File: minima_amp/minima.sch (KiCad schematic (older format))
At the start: 40 parts, among them J1 input, J2 output, J3 powersupply, U1 LM1875

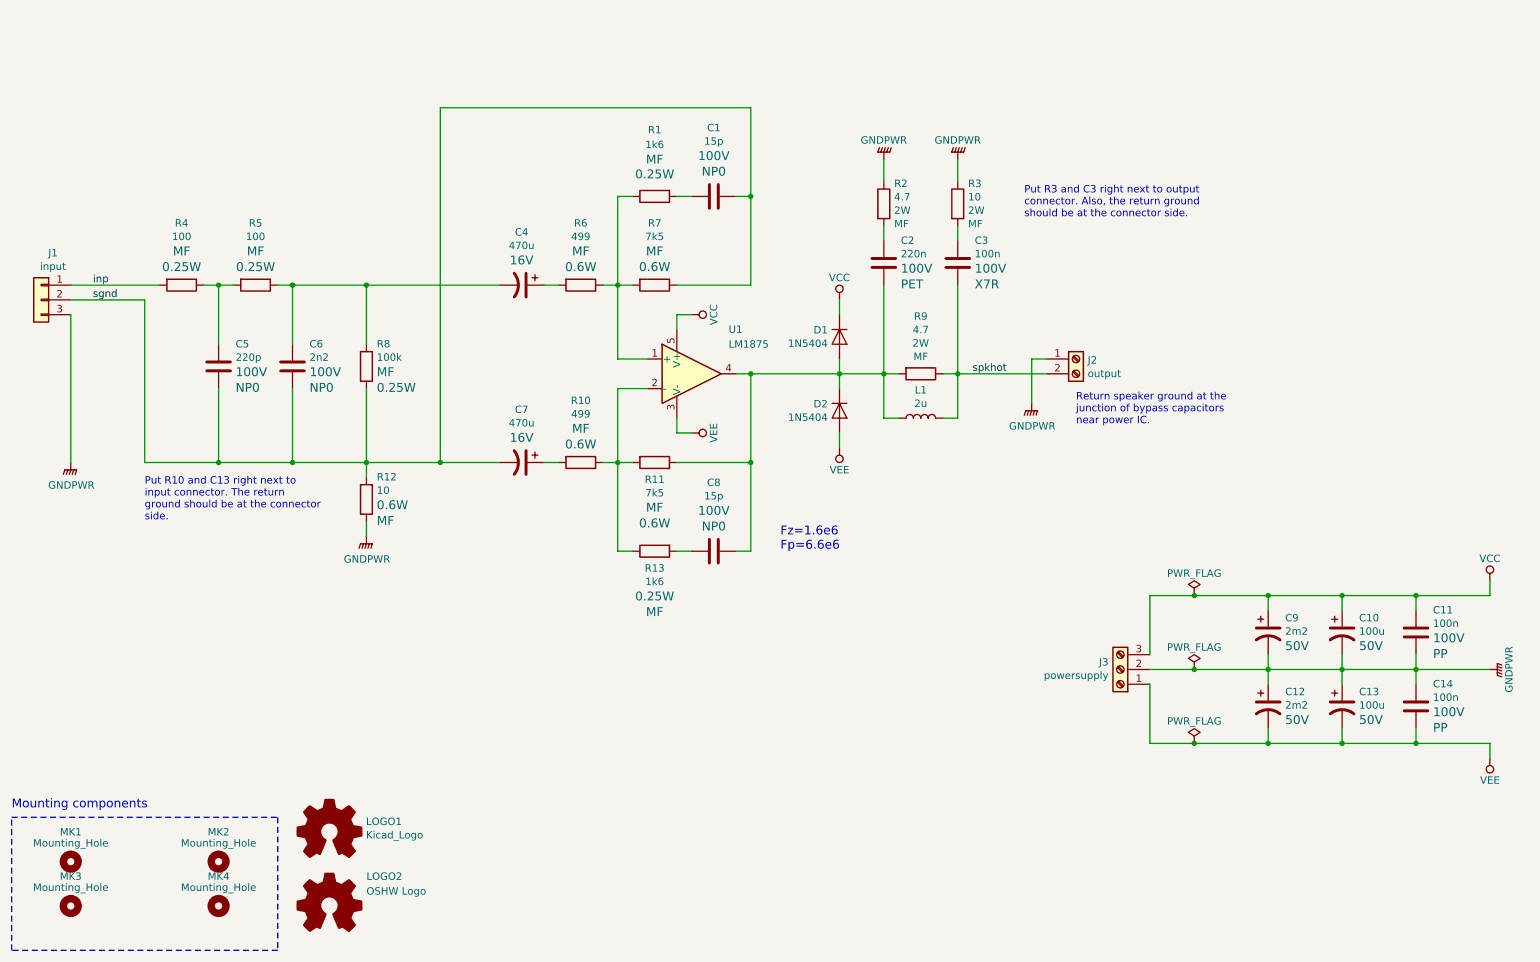
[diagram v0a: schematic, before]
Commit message: Using designators as specified in README.rst
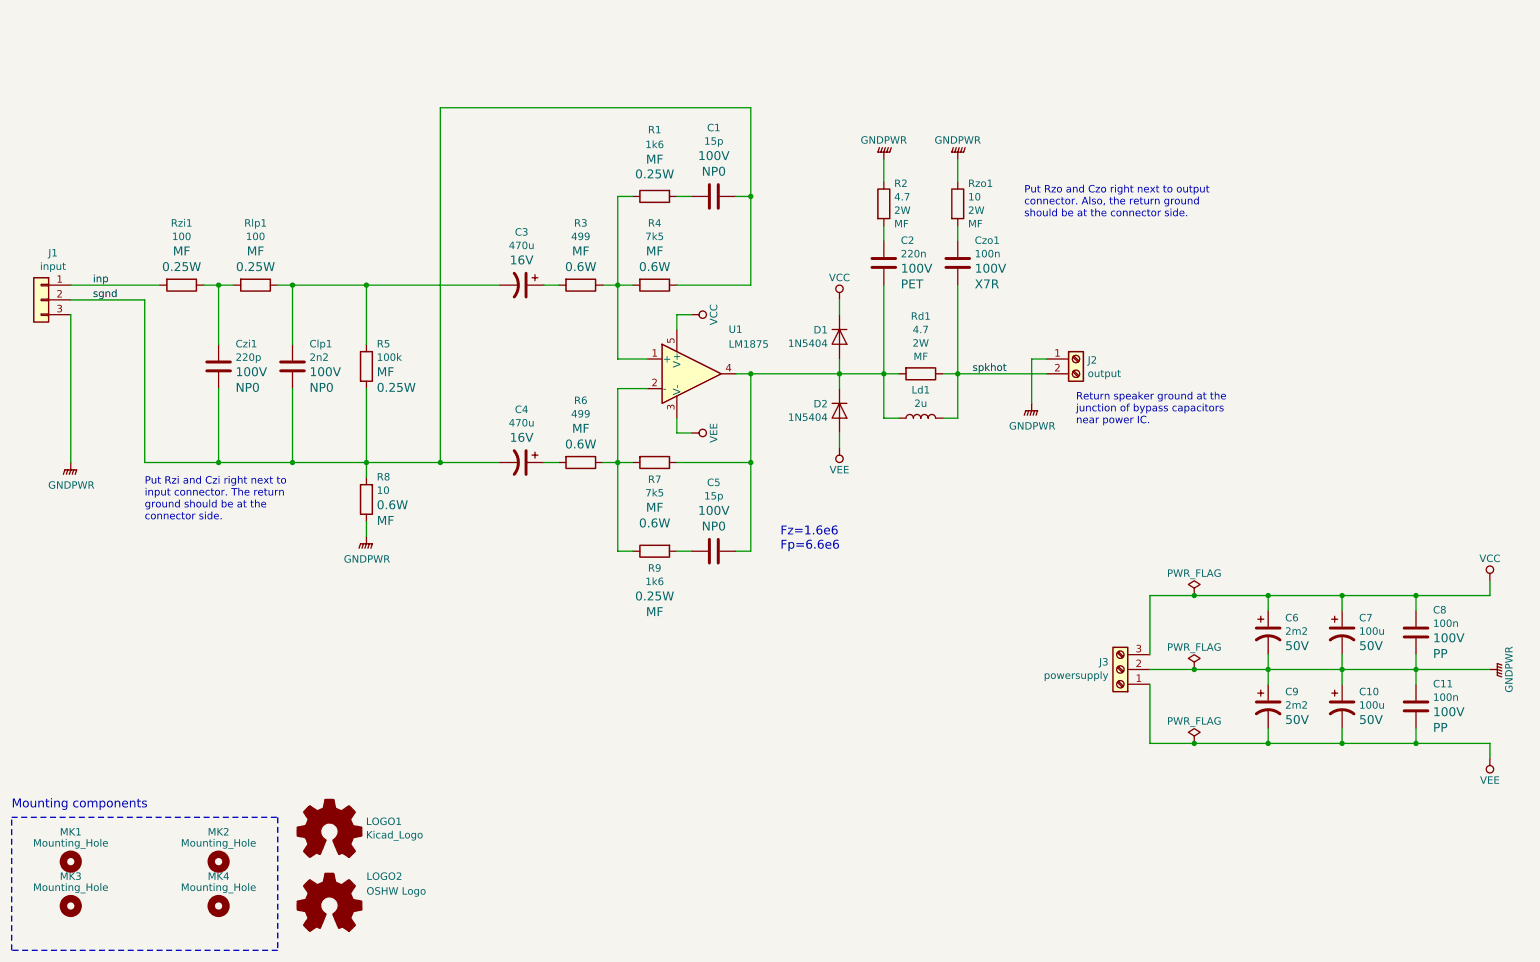
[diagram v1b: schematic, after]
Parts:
- renumbered C13 to C10, C14 to C11, C4 to C3, C7 to C4, C8 to C5, C9 to C6, C10 to C7, C11 to C8, C12 to C9, C6 to Clp1, C5 to Czi1, C3 to Czo1, L1 to Ld1, R6 to R3, R7 to R4, R8 to R5, R10 to R6, R11 to R7, R12 to R8, R13 to R9, R9 to Rd1, R5 to Rlp1, R4 to Rzi1, R3 to Rzo1
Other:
- note added: "Put Rzi and Czi right next to\ninput connector. The return\nground should be at the\nconnector side."
- note added: "Put Rzo and Czo right next to output \nconnector. Also, the return ground \nshould be at the connector side."
- note removed: "Put R10 and C13 right next to\ninput connector. The return\nground should be at the connector\nside."
- note removed: "Put R3 and C3 right next to output \nconnector. Also, the return ground \nshould be at the connector side."
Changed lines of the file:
@@
 Return speaker ground at the\njunction of bypass capacitors \nnear power IC.
 $Comp
-L Device:C C?
+L Device:C Clp?
 U 1 1 5B6E6214
 P 2700 3550
-AR Path="/5B57B0FA/5B6E6214" Ref="C?"  Part="1"
-AR Path="/5B6E6214" Ref="C6"  Part="1"
-F 0 "C6" H 2815 3702 50  0000 L CNN
+AR Path="/5B57B0FA/5B6E6214" Ref="Clp?"  Part="1"
+AR Path="/5B6E6214" Ref="Clp1"  Part="1"
+F 0 "Clp1" H 2815 3702 50  0000 L CNN
 F 1 "2n2" H 2815 3611 50  0000 L CNN
 F 2 "Capacitor_THT:C_Disc_D4.3mm_W1.9mm_P5.00mm" H 2738 3400 50  0001 C CNN
@@
 $EndComp
 $Comp
-L Device:C C?
+L Device:C Czi?
 U 1 1 5B6E621F
 P 2200 3550
-AR Path="/5B57B0FA/5B6E621F" Ref="C?"  Part="1"
-AR Path="/5B6E621F" Ref="C5"  Part="1"
-F 0 "C5" H 2315 3702 50  0000 L CNN
+AR Path="/5B57B0FA/5B6E621F" Ref="Czi?"  Part="1"
+AR Path="/5B6E621F" Ref="Czi1"  Part="1"
+F 0 "Czi1" H 2315 3702 50  0000 L CNN
 F 1 "220p" H 2315 3611 50  0000 L CNN
 F 2 "Capacitor_THT:C_Disc_D4.3mm_W1.9mm_P5.00mm" H 2238 3400 50  0001 C CNN
@@
 $EndComp
 $Comp
-L Device:R R?
+L Device:R Rzi?
 U 1 1 5B6E622C
 P 1950 3000
-AR Path="/5B57B0FA/5B6E622C" Ref="R?"  Part="1"
-AR Path="/5B6E622C" Ref="R4"  Part="1"
-F 0 "R4" V 1531 3000 50  0000 C CNN
+AR Path="/5B57B0FA/5B6E622C" Ref="Rzi?"  Part="1"
+AR Path="/5B6E622C" Ref="Rzi1"  Part="1"
+F 0 "Rzi1" V 1531 3000 50  0000 C CNN
 F 1 "100" V 1622 3000 50  0000 C CNN
 F 2 "Resistor_THT:R_Axial_DIN0207_L6.3mm_D2.5mm_P10.16mm_Horizontal" V 1880 3000 50  0001 C CNN
@@
 $EndComp
 $Comp
-L Device:R R?
+L Device:R Rlp?
 U 1 1 5B6E6237
 P 2450 3000
-AR Path="/5B57B0FA/5B6E6237" Ref="R?"  Part="1"
-AR Path="/5B6E6237" Ref="R5"  Part="1"
-F 0 "R5" V 2031 3000 50  0000 C CNN
+AR Path="/5B57B0FA/5B6E6237" Ref="Rlp?"  Part="1"
+AR Path="/5B6E6237" Ref="Rlp1"  Part="1"
+F 0 "Rlp1" V 2031 3000 50  0000 C CNN
 F 1 "100" V 2122 3000 50  0000 C CNN
 F 2 "Resistor_THT:R_Axial_DIN0207_L6.3mm_D2.5mm_P10.16mm_Horizontal" V 2380 3000 50  0001 C CNN
@@
 P 3200 4450
 AR Path="/5B57B0FA/5B6E6242" Ref="R?"  Part="1"
-AR Path="/5B6E6242" Ref="R12"  Part="1"
-F 0 "R12" H 3130 4298 50  0000 R CNN
+AR Path="/5B6E6242" Ref="R8"  Part="1"
+F 0 "R8" H 3130 4298 50  0000 R CNN
 F 1 "10" H 3130 4389 50  0000 R CNN
 F 2 "Resistor_THT:R_Axial_DIN0207_L6.3mm_D2.5mm_P10.16mm_Horizontal" V 3130 4450 50  0001 C CNN
@@
 P 3200 3550
 AR Path="/5B57B0FA/5B6E625B" Ref="R?"  Part="1"
-AR Path="/5B6E625B" Ref="R8"  Part="1"
-F 0 "R8" H 3270 3702 50  0000 L CNN
+AR Path="/5B6E625B" Ref="R5"  Part="1"
+F 0 "R5" H 3270 3702 50  0000 L CNN
 F 1 "100k" H 3270 3611 50  0000 L CNN
 F 2 "Resistor_THT:R_Axial_DIN0207_L6.3mm_D2.5mm_P10.16mm_Horizontal" V 3130 3550 50  0001 C CNN
@@
 $EndComp
 Text Notes 1700 4600 0    50   ~ 0
-Put R10 and C13 right next to\ninput connector. The return\nground should be at the connector\nside.
+Put Rzi and Czi right next to\ninput connector. The return\nground should be at the\nconnector side.
 Text Label 1350 3100 0    50   ~ 0
 sgnd
@@
 P 10300 5350
 AR Path="/5ABAAF3C/5B6EB783" Ref="C?"  Part="1"
-AR Path="/5B6EB783" Ref="C11"  Part="1"
-F 0 "C11" H 10415 5502 50  0000 L CNN
+AR Path="/5B6EB783" Ref="C8"  Part="1"
+F 0 "C8" H 10415 5502 50  0000 L CNN
 F 1 "100n" H 10415 5411 50  0000 L CNN
 F 2 "Capacitor_THT:C_Rect_L7.0mm_W3.5mm_P5.00mm" H 10338 5200 50  0001 C CNN
@@
 P 9800 5350
 AR Path="/5ABAAF3C/5B6EB78D" Ref="C?"  Part="1"
-AR Path="/5B6EB78D" Ref="C10"  Part="1"
-F 0 "C10" H 9915 5449 50  0000 L CNN
+AR Path="/5B6EB78D" Ref="C7"  Part="1"
+F 0 "C7" H 9915 5449 50  0000 L CNN
 F 1 "100u" H 9915 5358 50  0000 L CNN
 F 2 "Capacitor_THT:CP_Radial_D8.0mm_P3.50mm" H 9800 5350 50  0001 C CNN
@@
 P 10300 5850
 AR Path="/5ABAAF3C/5B6EB7B5" Ref="C?"  Part="1"
-AR Path="/5B6EB7B5" Ref="C14"  Part="1"
-F 0 "C14" H 10415 6002 50  0000 L CNN
+AR Path="/5B6EB7B5" Ref="C11"  Part="1"
+F 0 "C11" H 10415 6002 50  0000 L CNN
 F 1 "100n" H 10415 5911 50  0000 L CNN
 F 2 "Capacitor_THT:C_Rect_L7.0mm_W3.5mm_P5.00mm" H 10338 5700 50  0001 C CNN
@@
 P 9800 5850
 AR Path="/5ABAAF3C/5B6EB7BF" Ref="C?"  Part="1"
-AR Path="/5B6EB7BF" Ref="C13"  Part="1"
-F 0 "C13" H 9915 5949 50  0000 L CNN
+AR Path="/5B6EB7BF" Ref="C10"  Part="1"
+F 0 "C10" H 9915 5949 50  0000 L CNN
 F 1 "100u" H 9915 5858 50  0000 L CNN
 F 2 "Capacitor_THT:CP_Radial_D8.0mm_P3.50mm" H 9800 5850 50  0001 C CNN
@@
 P 9300 5350
 AR Path="/5ABAAF67/5B6EC2C2" Ref="C?"  Part="1"
-AR Path="/5B6EC2C2" Ref="C9"  Part="1"
-F 0 "C9" H 9415 5449 50  0000 L CNN
+AR Path="/5B6EC2C2" Ref="C6"  Part="1"
+F 0 "C6" H 9415 5449 50  0000 L CNN
 F 1 "2m2" H 9415 5358 50  0000 L CNN
 F 2 "Capacitor_THT:CP_Radial_D16.0mm_P7.50mm" H 9300 5350 50  0001 C CNN
@@
 P 9300 5850
 AR Path="/5ABAAF67/5B6EC310" Ref="C?"  Part="1"
-AR Path="/5B6EC310" Ref="C12"  Part="1"
-F 0 "C12" H 9415 5949 50  0000 L CNN
+AR Path="/5B6EC310" Ref="C9"  Part="1"
+F 0 "C9" H 9415 5949 50  0000 L CNN
 F 1 "2m2" H 9415 5858 50  0000 L CNN
 F 2 "Capacitor_THT:CP_Radial_D16.0mm_P7.50mm" H 9300 5850 50  0001 C CNN
@@
 $EndComp
 $Comp
-L Device:R R?
+L Device:R Rd?
 U 1 1 5B6FAE68
 P 6950 3600
-AR Path="/5ABAAF3C/5B6FAE68" Ref="R?"  Part="1"
-AR Path="/5B6FAE68" Ref="R9"  Part="1"
-F 0 "R9" V 6561 3600 50  0000 C CNN
+AR Path="/5ABAAF3C/5B6FAE68" Ref="Rd?"  Part="1"
+AR Path="/5B6FAE68" Ref="Rd1"  Part="1"
+F 0 "Rd1" V 6561 3600 50  0000 C CNN
 F 1 "4.7" V 6652 3600 50  0000 C CNN
 F 2 "Resistor_THT:R_Axial_DIN0411_L9.9mm_D3.6mm_P15.24mm_Horizontal" V 6880 3600 50  0001 C CNN
@@
 $EndComp
 $Comp
-L Device:L L?
+L Device:L Ld?
 U 1 1 5B6FAE6F
 P 6950 3900
-AR Path="/5ABAAF3C/5B6FAE6F" Ref="L?"  Part="1"
-AR Path="/5B6FAE6F" Ref="L1"  Part="1"
-F 0 "L1" V 7140 3900 50  0000 C CNN
+AR Path="/5ABAAF3C/5B6FAE6F" Ref="Ld?"  Part="1"
+AR Path="/5B6FAE6F" Ref="Ld1"  Part="1"
+F 0 "Ld1" V 7140 3900 50  0000 C CNN
 F 1 "2u" V 7049 3900 50  0000 C CNN
 F 2 "Inductor_THT:L_Axial_L12.0mm_D5.0mm_P15.24mm_Horizontal_Fastron_MISC" H 6950 3900 50  0001 C CNN
@@
 	6700 3900 6800 3900
 $Comp
-L Device:R R?
+L Device:R Rzo?
 U 1 1 5B6FAE7C
 P 7200 2450
-AR Path="/5ABAAF3C/5B6FAE7C" Ref="R?"  Part="1"
-AR Path="/5B6FAE7C" Ref="R3"  Part="1"
-F 0 "R3" H 7270 2587 50  0000 L CNN
+AR Path="/5ABAAF3C/5B6FAE7C" Ref="Rzo?"  Part="1"
+AR Path="/5B6FAE7C" Ref="Rzo1"  Part="1"
+F 0 "Rzo1" H 7270 2587 50  0000 L CNN
 F 1 "10" H 7270 2496 50  0000 L CNN
 F 2 "Resistor_THT:R_Axial_DIN0411_L9.9mm_D3.6mm_P15.24mm_Horizontal" V 7130 2450 50  0001 C CNN
@@
 P 4250 3000
 AR Path="/5ABAAF3C/5B6FAE98" Ref="C?"  Part="1"
-AR Path="/5B6FAE98" Ref="C4"  Part="1"
-F 0 "C4" V 3892 3000 50  0000 C CNN
+AR Path="/5B6FAE98" Ref="C3"  Part="1"
+F 0 "C3" V 3892 3000 50  0000 C CNN
 F 1 "470u" V 3983 3000 50  0000 C CNN
 F 2 "Capacitor_THT:CP_Radial_D8.0mm_P3.50mm" H 4250 3000 50  0001 C CNN
@@
 P 5150 4800
 AR Path="/5ABAAF3C/5B6FAEAE" Ref="R?"  Part="1"
-AR Path="/5B6FAEAE" Ref="R13"  Part="1"
-F 0 "R13" V 5265 4800 50  0000 C CNN
+AR Path="/5B6FAEAE" Ref="R9"  Part="1"
+F 0 "R9" V 5265 4800 50  0000 C CNN
 F 1 "1k6" V 5356 4800 50  0000 C CNN
 F 2 "Resistor_THT:R_Axial_DIN0207_L6.3mm_D2.5mm_P10.16mm_Horizontal" V 5080 4800 50  0001 C CNN
@@
 P 5550 4800
 AR Path="/5ABAAF3C/5B6FAEC1" Ref="C?"  Part="1"
-AR Path="/5B6FAEC1" Ref="C8"  Part="1"
-F 0 "C8" V 5086 4800 50  0000 C CNN
+AR Path="/5B6FAEC1" Ref="C5"  Part="1"
+F 0 "C5" V 5086 4800 50  0000 C CNN
 F 1 "15p" V 5177 4800 50  0000 C CNN
 F 2 "Capacitor_THT:C_Disc_D3.4mm_W2.1mm_P2.50mm" H 5588 4650 50  0001 C CNN
@@
 P 4250 4200
 AR Path="/5ABAAF3C/5B6FAED8" Ref="C?"  Part="1"
-AR Path="/5B6FAED8" Ref="C7"  Part="1"
-F 0 "C7" V 3892 4200 50  0000 C CNN
+AR Path="/5B6FAED8" Ref="C4"  Part="1"
+F 0 "C4" V 3892 4200 50  0000 C CNN
 F 1 "470u" V 3983 4200 50  0000 C CNN
 F 2 "Capacitor_THT:CP_Radial_D8.0mm_P3.50mm" H 4250 4200 50  0001 C CNN
@@
 P 4650 4200
 AR Path="/5ABAAF3C/5B6FAEE5" Ref="R?"  Part="1"
-AR Path="/5B6FAEE5" Ref="R10"  Part="1"
-F 0 "R10" V 4231 4200 50  0000 C CNN
+AR Path="/5B6FAEE5" Ref="R6"  Part="1"
+F 0 "R6" V 4231 4200 50  0000 C CNN
 F 1 "499" V 4322 4200 50  0000 C CNN
 F 2 "Resistor_THT:R_Axial_DIN0207_L6.3mm_D2.5mm_P10.16mm_Horizontal" V 4580 4200 50  0001 C CNN
@@
 P 5150 3000
 AR Path="/5ABAAF3C/5B6FAEF0" Ref="R?"  Part="1"
-AR Path="/5B6FAEF0" Ref="R7"  Part="1"
-F 0 "R7" V 4731 3000 50  0000 C CNN
+AR Path="/5B6FAEF0" Ref="R4"  Part="1"
+F 0 "R4" V 4731 3000 50  0000 C CNN
 F 1 "7k5" V 4822 3000 50  0000 C CNN
 F 2 "Resistor_THT:R_Axial_DIN0207_L6.3mm_D2.5mm_P10.16mm_Horizontal" V 5080 3000 50  0001 C CNN
@@
 P 5150 4200
 AR Path="/5ABAAF3C/5B6FAEFB" Ref="R?"  Part="1"
-AR Path="/5B6FAEFB" Ref="R11"  Part="1"
-F 0 "R11" V 5265 4200 50  0000 C CNN
+AR Path="/5B6FAEFB" Ref="R7"  Part="1"
+F 0 "R7" V 5265 4200 50  0000 C CNN
 F 1 "7k5" V 5356 4200 50  0000 C CNN
 F 2 "Resistor_THT:R_Axial_DIN0207_L6.3mm_D2.5mm_P10.16mm_Horizontal" V 5080 4200 50  0001 C CNN
@@
 P 4650 3000
 AR Path="/5ABAAF3C/5B6FAF30" Ref="R?"  Part="1"
-AR Path="/5B6FAF30" Ref="R6"  Part="1"
-F 0 "R6" V 4231 3000 50  0000 C CNN
+AR Path="/5B6FAF30" Ref="R3"  Part="1"
+F 0 "R3" V 4231 3000 50  0000 C CNN
 F 1 "499" V 4322 3000 50  0000 C CNN
 F 2 "Resistor_THT:R_Axial_DIN0207_L6.3mm_D2.5mm_P10.16mm_Horizontal" V 4580 3000 50  0001 C CNN
@@
 	7200 2300 7200 2150
 $Comp
-L Device:C C?
+L Device:C Czo?
 U 1 1 5B6FAF6B
 P 7200 2850
-AR Path="/5ABAAF3C/5B6FAF6B" Ref="C?"  Part="1"
-AR Path="/5B6FAF6B" Ref="C3"  Part="1"
-F 0 "C3" H 7315 3002 50  0000 L CNN
+AR Path="/5ABAAF3C/5B6FAF6B" Ref="Czo?"  Part="1"
+AR Path="/5B6FAF6B" Ref="Czo1"  Part="1"
+F 0 "Czo1" H 7315 3002 50  0000 L CNN
 F 1 "100n" H 7315 2911 50  0000 L CNN
 F 2 "Capacitor_THT:C_Disc_D5.1mm_W3.2mm_P5.00mm" H 7238 2700 50  0001 C CNN
@@
 	7200 2600 7200 2700
 Text Notes 7650 2550 0    50   ~ 0
-Put R3 and C3 right next to output \nconnector. Also, the return ground \nshould be at the connector side.
+Put Rzo and Czo right next to output \nconnector. Also, the return ground \nshould be at the connector side.
 Wire Wire Line
 	3200 3000 4100 3000

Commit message: Using Pluggable Terminal Block
Signed-off-by: Nenad Radulovic <nenad.b.radulovic@gmail.com>
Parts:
- J1: footprint TerminalBlock_Phoenix:TerminalBlock_Phoenix_PT-1,5-3-3.5-H_1x03_P3.50mm_Horizontal -> Connector_Phoenix_MC:PhoenixContact_MCV_1,5_3-G-3.5_1x03_P3.50mm_Vertical; Manufacturer Phoenix:MKDS1/3-3,5 -> Phoenix:1843619; Vendor Farnell:2478587 -> Farnell:3704828
- J2: footprint TerminalBlock_Phoenix:TerminalBlock_Phoenix_MKDS-3-2-5.08_1x02_P5.08mm_Horizontal -> Connector_Phoenix_MC:PhoenixContact_MCV_1,5_2-G-3.81_1x02_P3.81mm_Vertical; Manufacturer Phoenix:MKDSN2,5/2-5.08 -> Phoenix:MCV 1,5/ 2-GF-3,81; Vendor Farnell:1792766 -> Farnell:1793055
- J3: footprint TerminalBlock_Phoenix:TerminalBlock_Phoenix_MKDS-3-3-5.08_1x03_P5.08mm_Horizontal -> Connector_Phoenix_MC:PhoenixContact_MCV_1,5_3-G-3.81_1x03_P3.81mm_Vertical; Manufacturer Phoenix:MKDSN2,5/3-5.08 -> Phoenix:1803439; Vendor Farnell:1792767 -> Farnell:3913089
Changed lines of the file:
@@
 F 0 "J2" H 8079 3492 50  0000 L CNN
 F 1 "output" H 8079 3401 50  0000 L CNN
-F 2 "TerminalBlock_Phoenix:TerminalBlock_Phoenix_MKDS-3-2-5.08_1x02_P5.08mm_Horizontal" H 8000 3500 50  0001 C CNN
-F 3 "http://www.farnell.com/datasheets/2325421.pdf" H 8000 3500 50  0001 C CNN
-F 4 "Farnell:1792766" H 8000 3500 60  0001 C CNN "Vendor"
-F 5 "Phoenix:MKDSN2,5/2-5.08" H 8000 3500 60  0001 C CNN "Manufacturer"
+F 2 "Connector_Phoenix_MC:PhoenixContact_MCV_1,5_2-G-3.81_1x02_P3.81mm_Vertical" H 8000 3500 50  0001 C CNN
+F 3 "http://www.farnell.com/datasheets/2133308.pdf" H 8000 3500 50  0001 C CNN
+F 4 "Farnell:1793055" H 8000 3500 60  0001 C CNN "Vendor"
+F 5 "Phoenix:MCV 1,5/ 2-GF-3,81 " H 8000 3500 60  0001 C CNN "Manufacturer"
 	1    8000 3500
 	1    0    0    -1
@@
 F 0 "J1" H 920 3417 50  0000 C CNN
 F 1 "input" H 920 3326 50  0000 C CNN
-F 2 "TerminalBlock_Phoenix:TerminalBlock_Phoenix_PT-1,5-3-3.5-H_1x03_P3.50mm_Horizontal" H 1000 3100 50  0001 C CNN
-F 3 "http://www.farnell.com/datasheets/2322648.pdf" H 1000 3100 50  0001 C CNN
-F 4 "Phoenix:MKDS1/3-3,5" H -1500 1200 50  0001 C CNN "Manufacturer"
-F 5 "Farnell:2478587" H -1500 1200 50  0001 C CNN "Vendor"
+F 2 "Connector_Phoenix_MC:PhoenixContact_MCV_1,5_3-G-3.5_1x03_P3.50mm_Vertical" H 1000 3100 50  0001 C CNN
+F 3 "http://www.farnell.com/datasheets/2309782.pdf" H 1000 3100 50  0001 C CNN
+F 4 "Phoenix:1843619" H -1500 1200 50  0001 C CNN "Manufacturer"
+F 5 "Farnell:3704828" H -1500 1200 50  0001 C CNN "Vendor"
 	1    1000 3100
 	-1   0    0    -1
@@
 F 0 "J3" H 8380 5550 50  0000 L CNN
 F 1 "powersupply" H 8380 5641 50  0000 L CNN
-F 2 "TerminalBlock_Phoenix:TerminalBlock_Phoenix_MKDS-3-3-5.08_1x03_P5.08mm_Horizontal" H 8300 5600 50  0001 C CNN
-F 3 "http://www.farnell.com/datasheets/2325422.pdf" H 8300 5600 50  0001 C CNN
-F 4 "Phoenix:MKDSN2,5/3-5.08" H 2750 1300 50  0001 C CNN "Manufacturer"
-F 5 "Farnell:1792767" H 2750 1300 50  0001 C CNN "Vendor"
+F 2 "Connector_Phoenix_MC:PhoenixContact_MCV_1,5_3-G-3.81_1x03_P3.81mm_Vertical" H 8300 5600 50  0001 C CNN
+F 3 "http://www.farnell.com/datasheets/2138271.pdf" H 8300 5600 50  0001 C CNN
+F 4 "Phoenix:1803439" H 2750 1300 50  0001 C CNN "Manufacturer"
+F 5 "Farnell:3913089" H 2750 1300 50  0001 C CNN "Vendor"
 	1    8300 5600
 	-1   0    0    1
